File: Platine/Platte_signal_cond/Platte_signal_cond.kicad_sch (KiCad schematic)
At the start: 28 parts, among them J1 Conn_01x06, J2 Conn_01x07_MountingPin

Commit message: Small correction. Everything finished
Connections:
- net +3.3VA: no longer J1.2 (Pin_2)
- net GNDA: now also J1.2 (Pin_2)
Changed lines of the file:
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@@
 	)
 	(junction
-		(at 138.43 95.25)
+		(at 114.3 95.25)
 		(diameter 0)
 		(color 0 0 0 0)
@@
 	(wire
 		(pts
+			(xy 113.03 95.25) (xy 114.3 95.25)
+		)
+		(stroke
+			(width 0)
+			(type default)
+		)
+	)
+	(wire
+		(pts
 			(xy 46.99 156.21) (xy 46.99 157.48)
 		)
@@
 		(pts
 			(xy 114.3 95.25) (xy 115.57 95.25)
-		)
-		(stroke
-			(width 0)
-			(type default)
-		)
-	)
-	(wire
-		(pts
-			(xy 138.43 95.25) (xy 142.24 95.25)
 		)
 		(stroke
@@
 	(text "Stecker (von draußen)"
 		(exclude_from_sim no)
-		(at 209.042 25.4 0)
+		(at 213.868 24.892 0)
 		(effects
 			(font
@@
 	)
 	(label "VPlatte(60V)"
-		(at 142.24 95.25 0)
-		(fields_autoplaced yes)
-		(effects
-			(font
-				(size 1.27 1.27)
-			)
-			(justify left bottom)
-		)
-	)
+		(at 113.03 95.25 180)
+		(fields_autoplaced yes)
+		(effects
+			(font
+				(size 1.27 1.27)
+			)
+			(justify right bottom)
+		)
+	)

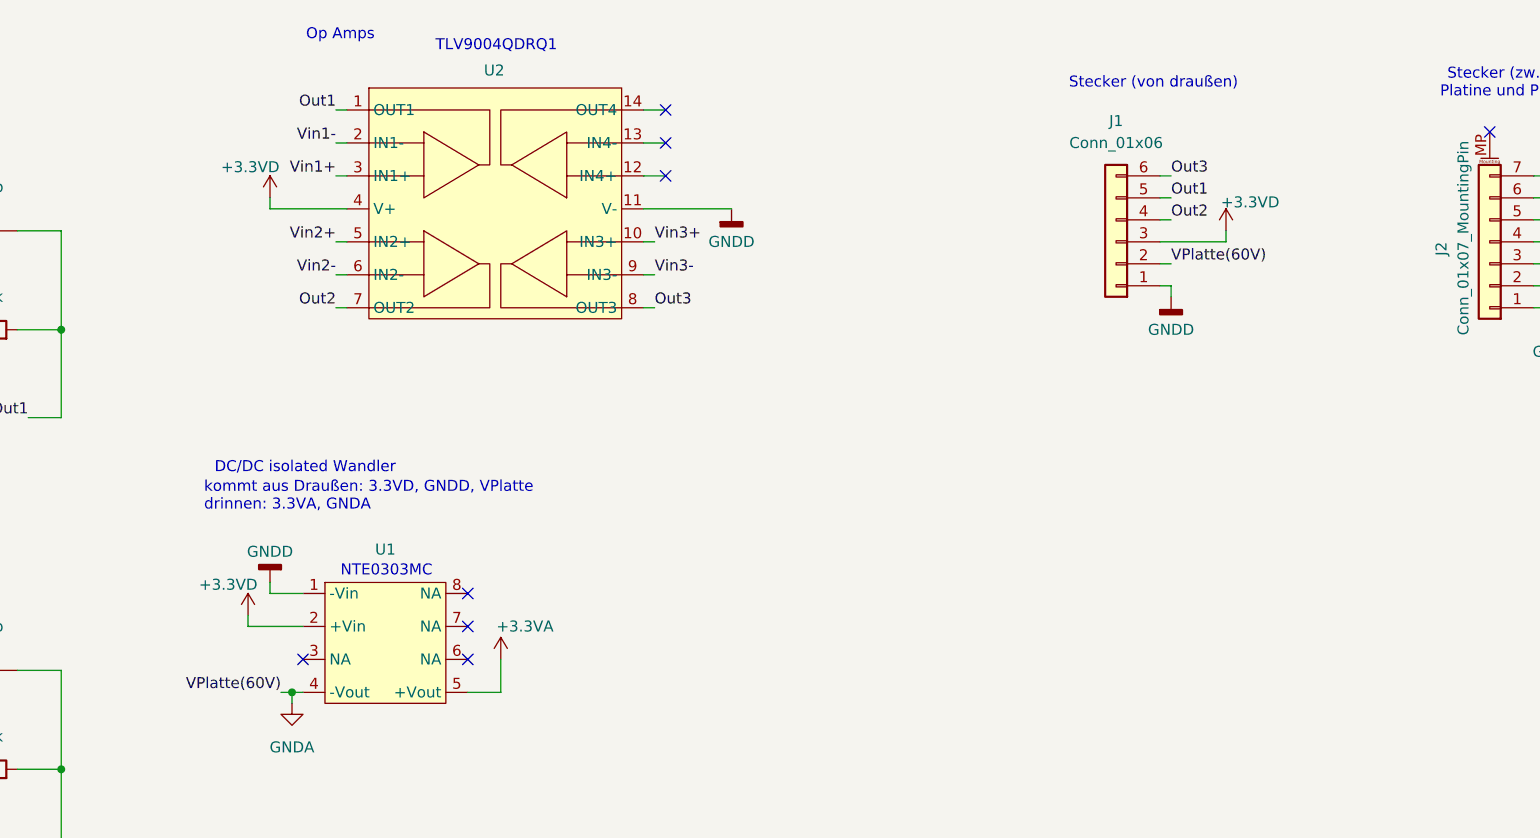
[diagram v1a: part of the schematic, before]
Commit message: Better shaping the Plates on the PCB
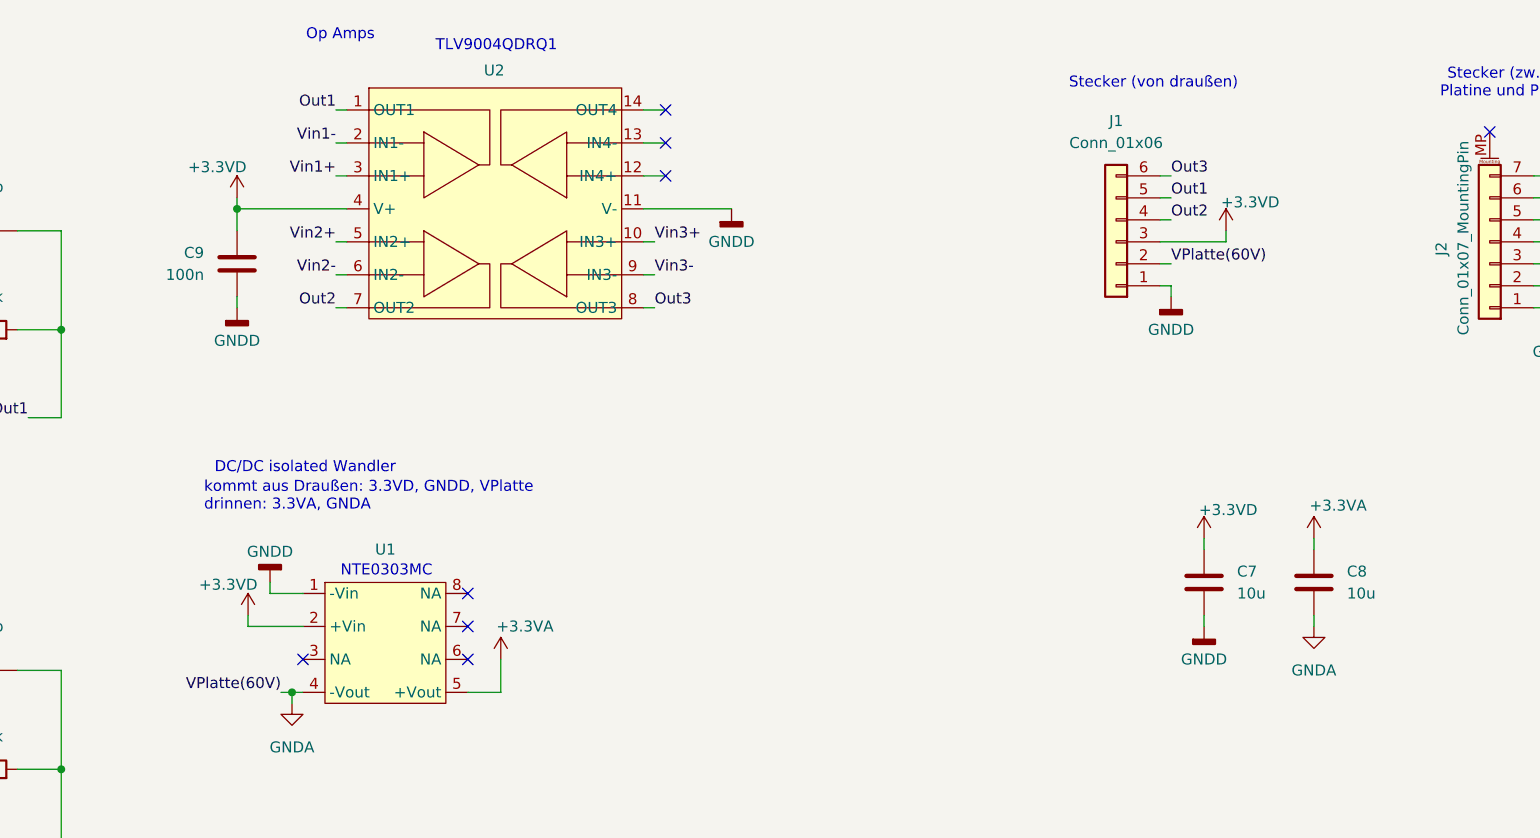
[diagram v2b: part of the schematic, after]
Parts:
- added C7, C8: 10u, Capacitor_SMD:C_0603_1608Metric_Pad1.08x0.95mm_HandSolder, symbol Device:C
- added C9: 100n, Capacitor_SMD:C_0603_1608Metric_Pad1.08x0.95mm_HandSolder, symbol Device:C
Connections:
- net +3.3VA: now also C8.2
- net +3.3VD: now also C7.2, C9.2
- net GNDA: now also C8.1
- net GNDD: now also C7.1, C9.1

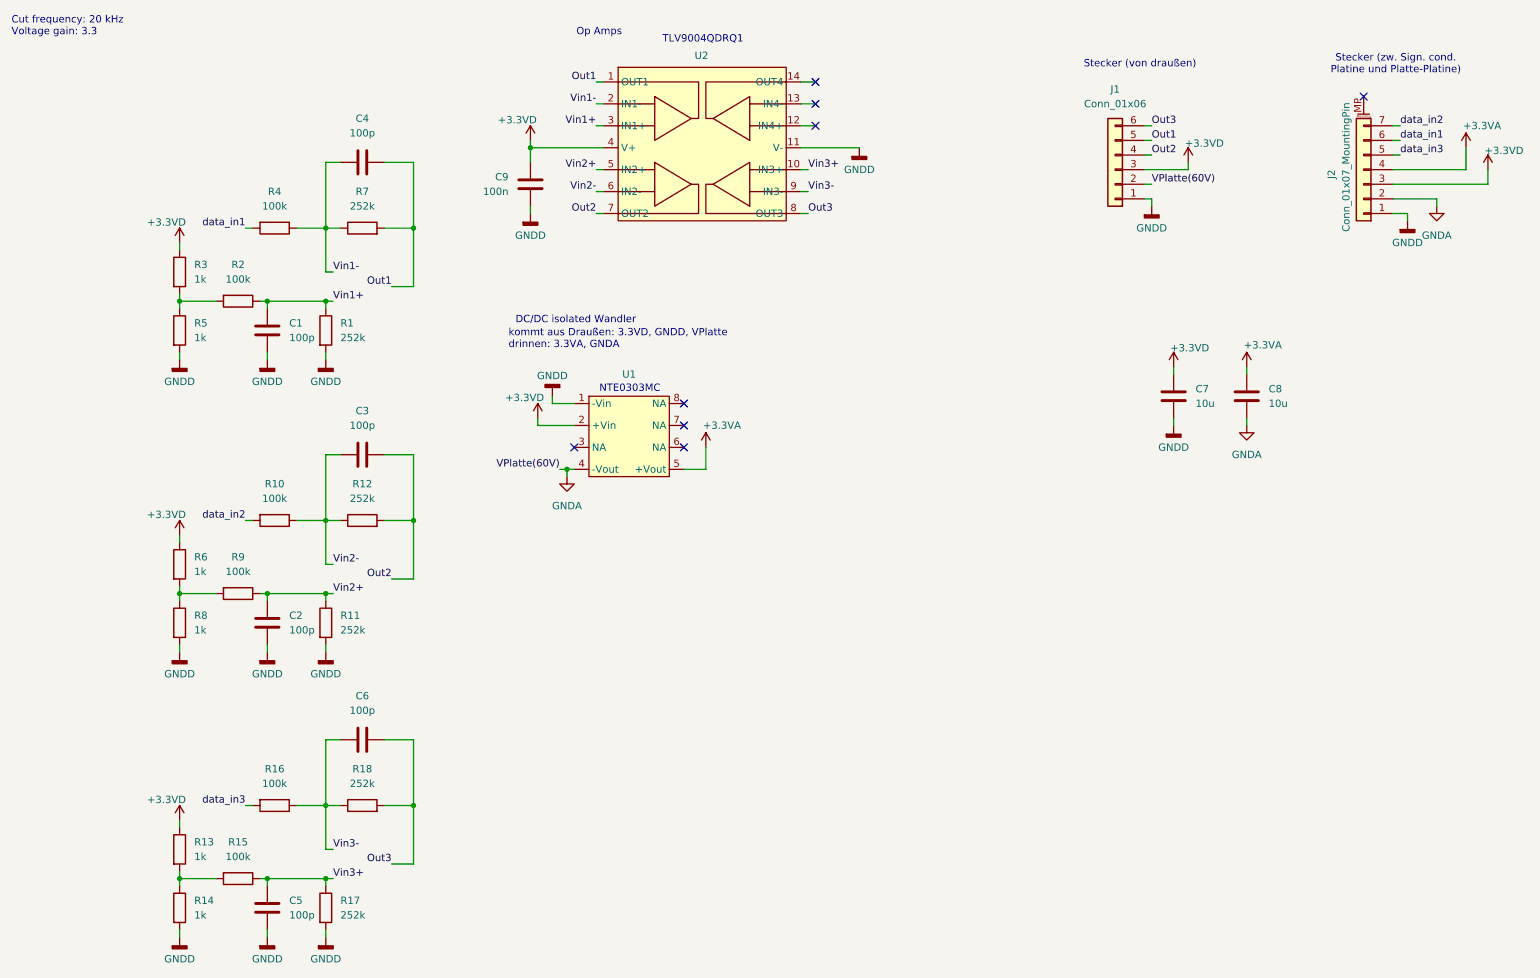
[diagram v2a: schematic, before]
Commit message: Updated Arduino code for reading test PCB
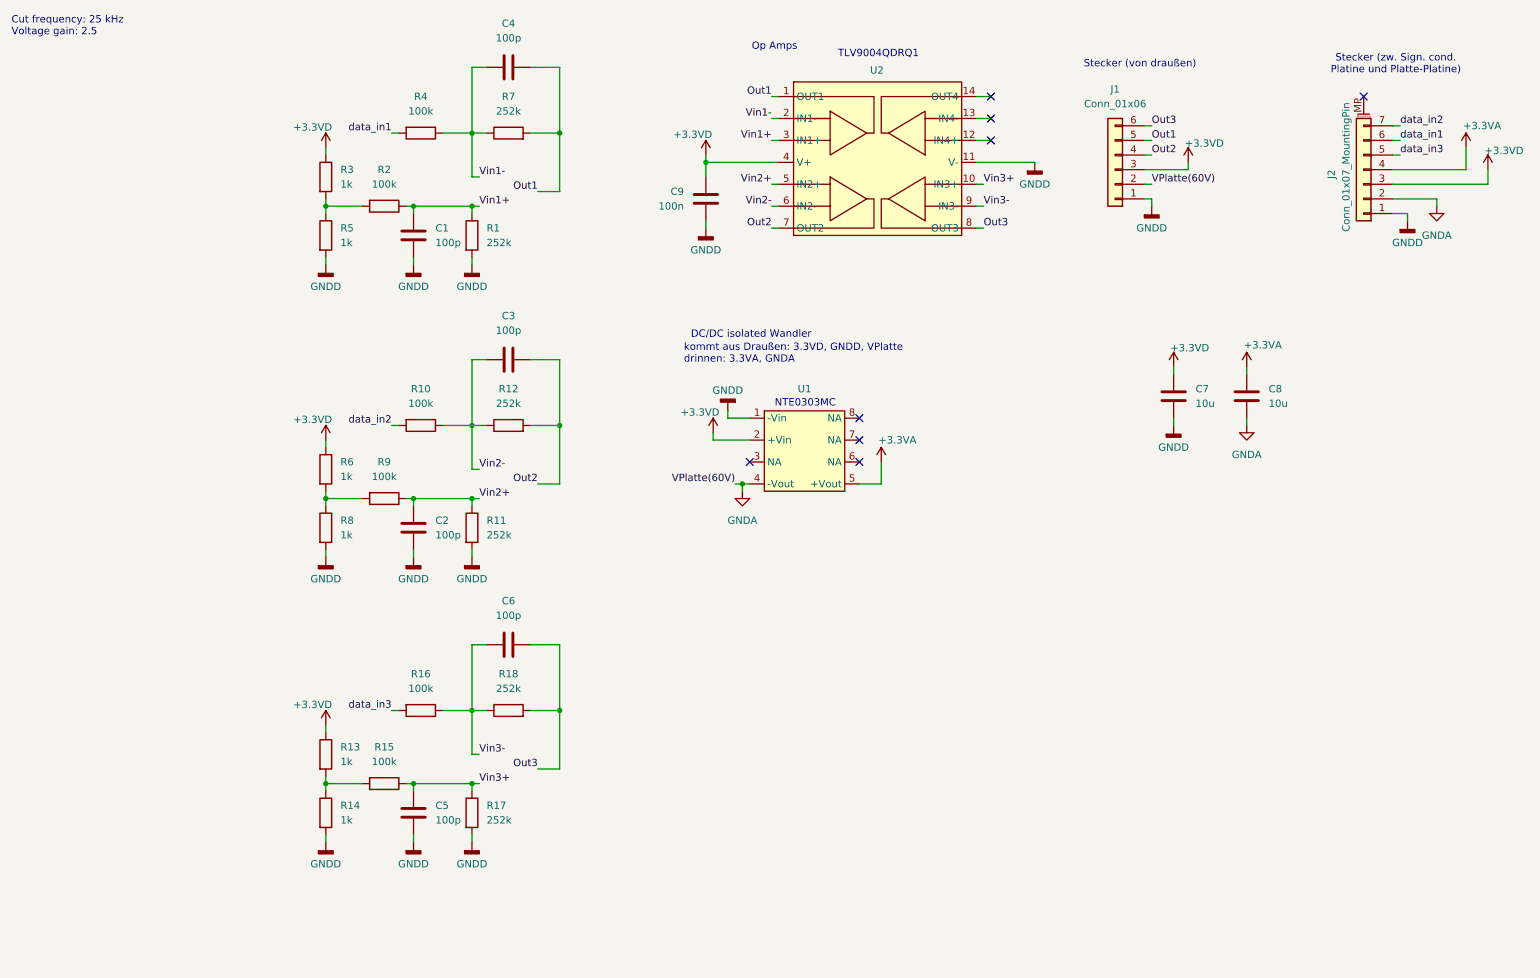
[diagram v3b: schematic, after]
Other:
- note added: "Cut frequency: 25 kHz Voltage gain: 2.5"
- note removed: "Cut frequency: 20 kHz Voltage gain: 3.3"
- moved on the sheet: C1, C2, C3, C4, C5, C6, C9, R1, R10, R11, R12, R13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
